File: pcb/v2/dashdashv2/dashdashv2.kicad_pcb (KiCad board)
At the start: 2 copper layers, 99 parts, among them J1 USB_B, J10 O2_CONN1, J11 BATT_CONN1, J12 OIL_CONN1, J13 OIL_TEMP1, J2 Tag connect, J3 Conn_01x04_Female, J4 Conn_01x04_Female, J5 SPEED_CONN1, J6 DISPLAY1, J7 RPM_CONN1, J8 TEMP1, J9 FUEL_CONN1, Q1 IRF540N, Q2 IRF540N, Q3 2N3904, U1 RP2040, U10 PCA9685PW, U11 MIC2940A-3.3WU, U12 SRV05-4, U13 LT4363IMS, U14 ADUM4160, U14 SRV05-4, U15 SRV05-4, U16 SRV05-4, U17 SRV05-4, U18 GL2576-3.3TA5R, U19 GL2576-5.0TA5R, U2 W25Q128JVS, U3 MCP2515-xSO, U4 TJA1042T3118, U5 TPD2E2U06, U6 SRV05-4, U7 25LCxxx, U8 SRV05-4, U9 MIC2940A-5.0WT, Y1 8MHz, Y2 12MHz

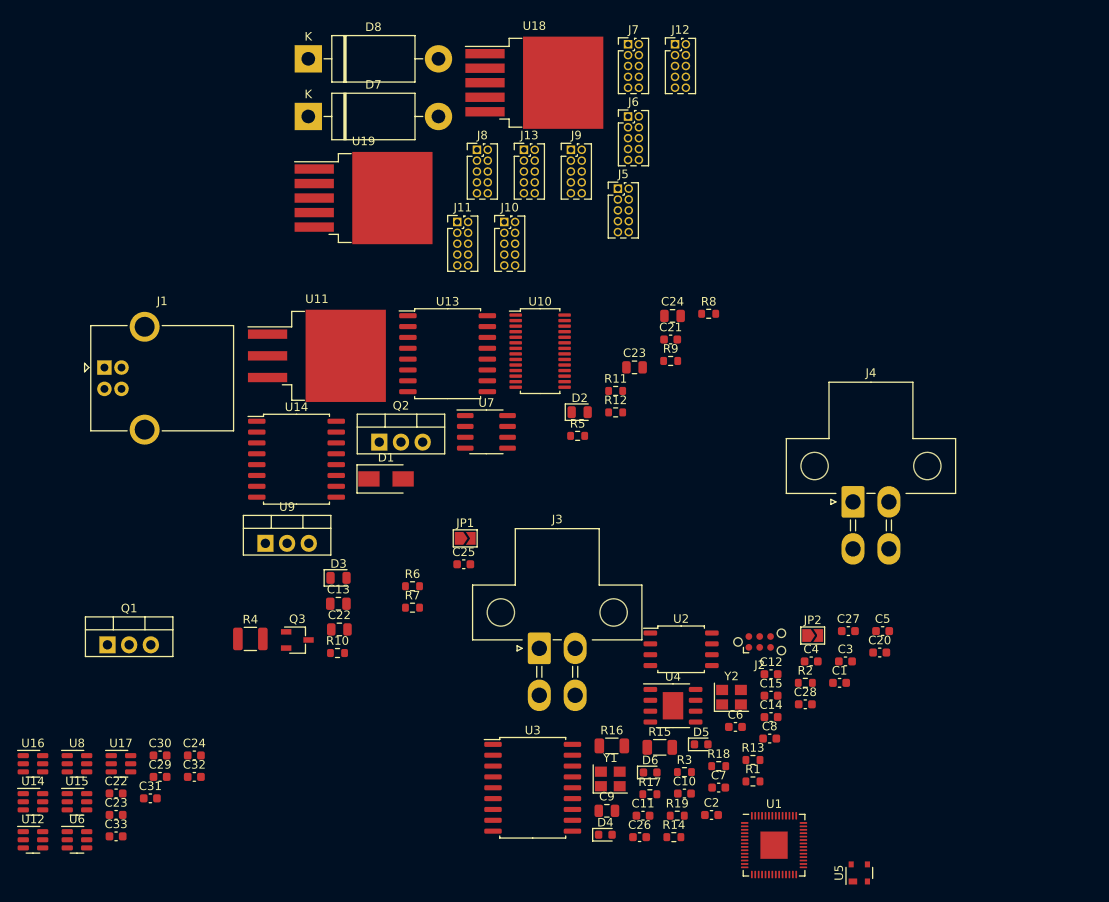
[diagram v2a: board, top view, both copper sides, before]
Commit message: routing can/usb/power/leds/flash
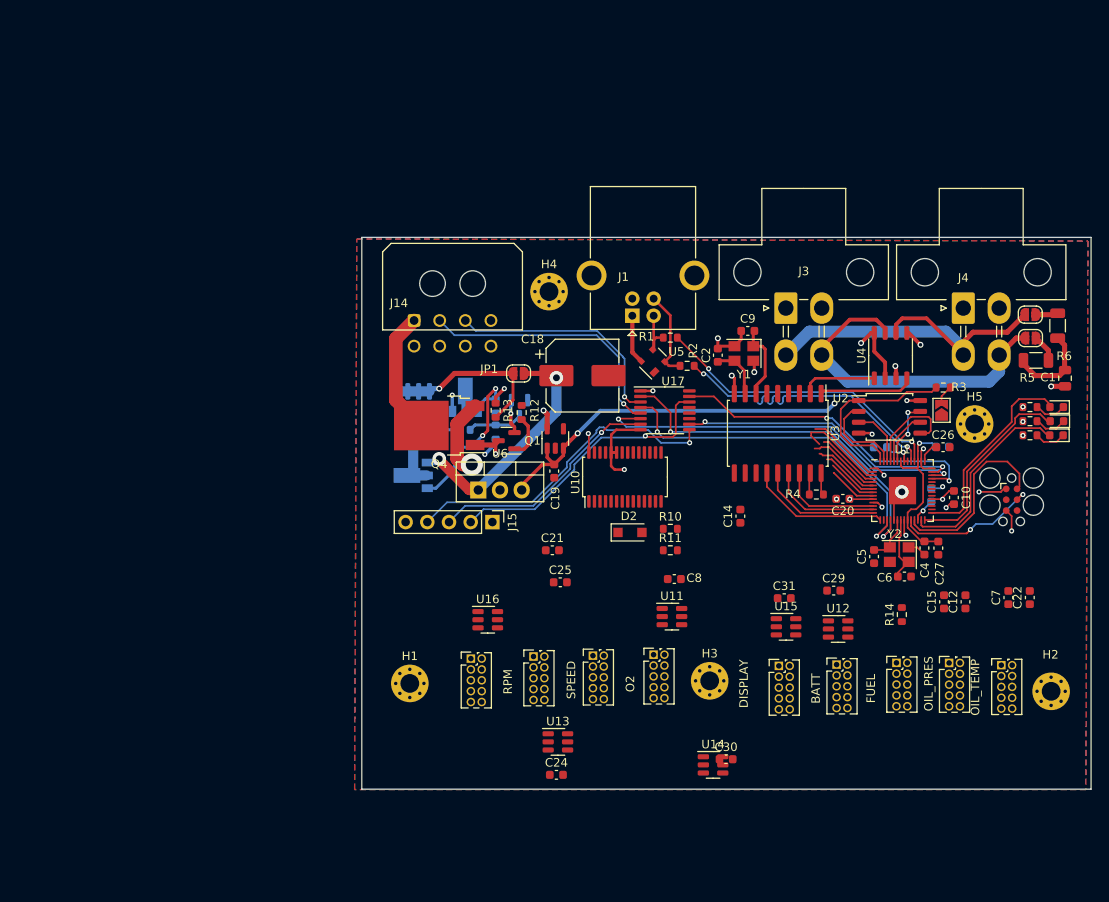
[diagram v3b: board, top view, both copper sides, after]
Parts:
- removed C13, C23: 100nF, Capacitor_SMD:C_0805_2012Metric
- removed the C22 at (136.1, 98.5)
- removed the C22 at (110.0, 117.8)
- removed C23, C33: 100nF, Capacitor_SMD:C_0603_1608Metric
- removed the C24 at (175.1, 61.8)
- removed the C24 at (119.2, 113.3)
- removed C3: 2.2uF, Capacitor_SMD:C_0603_1608Metric
- removed D3: 1N4148, Diode_SMD:D_0805_2012Metric
- removed D7, D8: 1N5822, Diode_THT:D_DO-201AD_P15.24mm_Horizontal
- removed R15, R16: 30R, Resistor_SMD:R_1206_3216Metric
- removed the U14 at (100.3, 118.7)
- removed the U14 at (131.1, 78.6)
- removed U18: GL2576-3.3TA5R, Package_TO_SOT_SMD:TO-263-5_TabPin3
- removed U19: GL2576-5.0TA5R, Package_TO_SOT_SMD:TO-263-5_TabPin3
- removed U7: 25LCxxx, Package_SO:SOIC-8_3.9x4.9mm_P1.27mm
- removed U9: MIC2940A-5.0WT, Package_TO_SOT_THT:TO-220-3_Vertical
- added C18: 120uF, Capacitor_SMD:CP_Elec_8x6.5, F.Cu at (164.6, 68.8)
- added C19: 100nF, Capacitor_SMD:C_0603_1608Metric, F.Cu at (161.3, 80.0)
- added C22: 100nF, Capacitor_SMD:C_0603_1608Metric, F.Cu at (217.0, 94.8)
- added C24: 100nF, Capacitor_SMD:C_0603_1608Metric, F.Cu at (161.5, 115.6)
- added H1: MountingHole, MountingHole:MountingHole_2.2mm_M2_Pad_Via, F.Cu at (144.4, 104.9)
- added H2: MountingHole, MountingHole:MountingHole_2.2mm_M2_Pad_Via, F.Cu at (219.5, 105.8)
- added H3: MountingHole, MountingHole:MountingHole_2.2mm_M2_Pad_Via, F.Cu at (179.5, 104.6)
- added H4: MountingHole, MountingHole:MountingHole_2.2mm_M2_Pad_Via, F.Cu at (160.7, 59.0)
- added H5: MountingHole, MountingHole:MountingHole_2.2mm_M2_Pad_Via, F.Cu at (210.5, 74.5)
- added J14: Conn_01x08, Connector_Molex:Molex_Micro-Fit_3.0_43045-0800_2x04_P3.00mm_Horizontal, F.Cu at (144.9, 62.4)
- added J15: Conn_01x05, Connector_PinHeader_2.54mm:PinHeader_1x05_P2.54mm_Vertical, F.Cu at (154.1, 86.0)
- added JP5: Jumper_2_Open, Jumper:SolderJumper-2_P1.3mm_Open_RoundedPad1.0x1.5mm, F.Cu at (217.0, 64.4)
- added JP6: Jumper_2_Open, Jumper:SolderJumper-2_P1.3mm_Open_RoundedPad1.0x1.5mm, F.Cu at (217.0, 61.7)
- added Q4: IRF9540N, Package_TO_SOT_SMD:TO-252-2, F.Cu at (147.8, 74.7)
- added Q5: MCQ9435-TP, Package_SO:SOIC-8_3.9x4.9mm_P1.27mm, B.Cu at (144.8, 73.2)
- added U14: SRV05-4, Package_TO_SOT_SMD:SOT-23-6, F.Cu at (179.9, 114.4)
- C1: value 30pF -> 4.7nF; footprint Capacitor_SMD:C_0603_1608Metric -> Capacitor_SMD:C_0805_2012Metric
- C11, C28, C32: moved to B.Cu
- C21: value 47nF -> 30pF
- C25: value 0.1uF -> 100nF
- C9: value 4.7nF -> 30pF; footprint Capacitor_SMD:C_0805_2012Metric -> Capacitor_SMD:C_0603_1608Metric
- D1: value SMAJ58CA -> BZX84C5V6LT1G; footprint Diode_SMD:D_SMA -> Package_TO_SOT_SMD:SOT-23; moved to B.Cu
- D2: value 1N4148 -> D_Zener; footprint Diode_SMD:D_0805_2012Metric -> Diode_SMD:D_SOD-123F
- J2: footprint Connector:Tag-Connect_TC2030-IDC-NL_2x03_P1.27mm_Vertical -> Connector:Tag-Connect_TC2030-IDC-FP_2x03_P1.27mm_Vertical
- JP1: footprint Jumper:SolderJumper-2_P1.3mm_Open_TrianglePad1.0x1.5mm -> Jumper:SolderJumper-2_P1.3mm_Open_RoundedPad1.0x1.5mm
- Q1: value IRF540N -> SS8050; footprint Package_TO_SOT_THT:TO-220-3_Vertical -> Package_TO_SOT_SMD:SOT-23
- Q2: value IRF540N -> 2PB1424,115; footprint Package_TO_SOT_THT:TO-220-3_Vertical -> Package_TO_SOT_SMD:SOT-89-3; moved to B.Cu
- Q3: value 2N3904 -> 2PB1424,115; footprint Package_TO_SOT_SMD:TSOT-23 -> Package_TO_SOT_SMD:SOT-89-3; moved to B.Cu
- R10: value 22r -> 5k
- R11: value 22r -> 1k
- R12: value 10K 1/10W -> 10k
- R4: value 0.01R -> 10k; footprint Resistor_SMD:R_1210_3225Metric -> Resistor_SMD:R_0603_1608Metric
- R5: value 57.6K 1/10W -> 60R; footprint Resistor_SMD:R_0603_1608Metric -> Resistor_SMD:R_1206_3216Metric
- R6: value 4.99K 1/10W -> 60R; footprint Resistor_SMD:R_0603_1608Metric -> Resistor_SMD:R_1206_3216Metric
- R7, R8: value 10R 1/10W -> 6k8; moved to B.Cu
- R9: value 1M 1/10W -> 2k7; moved to B.Cu
- U11: value MIC2940A-3.3WU -> SRV05-4; footprint Package_TO_SOT_SMD:TO-263-3_TabPin2 -> Package_TO_SOT_SMD:SOT-23-6
- U13: value LT4363IMS -> SRV05-4; footprint Package_SO:SOIC-16W_7.5x10.3mm_P1.27mm -> Package_TO_SOT_SMD:SOT-23-6
- U17: value SRV05-4 -> 4050; footprint Package_TO_SOT_SMD:SOT-23-6 -> Package_SO:TSSOP-16_4.4x5mm_P0.65mm
- U6: value SRV05-4 -> LM7805_TO220; footprint Package_TO_SOT_SMD:SOT-23-6 -> Package_TO_SOT_THT:TO-220-3_Vertical
- U8: value SRV05-4 -> LP5907MFX-3.3; footprint Package_TO_SOT_SMD:SOT-23-6 -> Package_TO_SOT_SMD:SOT-23-5
- moved U12 97.4 mm to (194.5, 98.5)
- moved C32 89.1 mm to (199.5, 77.2)
- moved U15 85.5 mm to (188.4, 98.2)
- moved C29 81.8 mm to (194.0, 94.0)
- moved R6 81.4 mm to (220.2, 63.0), turned to 90 degrees
- moved J12 79.2 mm to (207.5, 102.5)
- moved C31 77.8 mm to (188.2, 94.9)
- moved J6 77.7 mm to (213.6, 102.7)
- moved U17 75.9 mm to (174.2, 72.9)
- moved J7 74.2 mm to (151.5, 102.0)
- moved J8 73.5 mm to (194.3, 102.7)
- moved D4 70.5 mm to (220.1, 75.8), turned to 180 degrees
- moved R4 68.4 mm to (192.0, 82.8)
- moved U8 67.7 mm to (161.4, 76.2), turned to 90 degrees
- moved C30 66.3 mm to (181.4, 113.7)
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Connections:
- net /PWM_BACK_FUEl renamed PWM_BACK_FUEl
- net Net-(R14-Pad1) renamed /QSPI_SS
- net Net-(U1-Pad51) renamed /QSPI_SD3
- net Net-(U1-Pad52) renamed /QSPI_SCLK
- net Net-(U1-Pad53) renamed /QSPI_SD0
- net Net-(U1-Pad54) renamed /QSPI_SD2
- net Net-(U1-Pad55) renamed /QSPI_SD1
- C1 pad 1: GND -> Net-(C1-Pad1)
- C1 pad 2: /CAN_CLOCK_A -> GND
- C2 pad 2: /CAN_CLOCK_B -> /CAN/CAN_CLOCK_A
- C21 pad 1: Net-(C21-Pad1) -> GND
- C21 pad 2: GND -> +3V3
- C25 pad 1: Net-(C25-Pad1) -> GND
- C25 pad 2: GND -> +3V3
- C28 pad 1: unconnected-(C28-Pad1) -> +1V1
- C7 pad 2: +3V3 -> Net-(C7-Pad2)
- C8 pad 1: GND -> Net-(C7-Pad2)
- C8 pad 2: +3V3 -> GND
- C9 pad 1: Net-(C9-Pad1) -> GND
- C9 pad 2: GND -> /CAN/CAN_CLOCK_B
- D1 pad 1: Net-(D1-Pad1) -> GND
- D1 pad 2: GND -> unconnected-(D1-Pad2)
- D2 pad 2: +12VA -> GND
- J10 pad 1: +5V -> +12LF
- J10 pad 2: +5V -> +12LF
- J10 pad 3: /CLK -> CLK
- J10 pad 4: /O2_CS -> O2_CS
- J10 pad 5: /MISO -> MISO
- J10 pad 7: /MOSI -> MOSI
- J10 pad 8: /PWM_BACK_O2 -> PWM_BACK_O2
- J11 pad 1: +5V -> +12LF
- J11 pad 2: +5V -> +12LF
- J11 pad 3: /CLK -> CLK
- J11 pad 4: /BATT_CS -> BATT_CS
- J11 pad 5: /MISO -> MISO
- J11 pad 7: /MOSI -> MOSI
- J11 pad 8: /PWM_BACK_BATT -> PWM_BACK_BATT
- J12 pad 1: +5V -> +12LF
- J12 pad 2: +5V -> +12LF
- J12 pad 3: /CLK -> CLK
- J12 pad 4: /OIL_CS -> OIL_CS
- J12 pad 5: /MISO -> MISO
- J12 pad 7: /MOSI -> MOSI
- J12 pad 8: /PWM_BACK_OIL -> PWM_BACK_OIL
- J13 pad 1: +5V -> +12LF
- J13 pad 2: +5V -> +12LF
- J13 pad 3: /CLK -> CLK
- J13 pad 4: /OIL_TEMP_CS -> OIL_TEMP_CS
- J13 pad 5: /MISO -> MISO
- J13 pad 7: /MOSI -> MOSI
- J13 pad 8: /PWM_BACK_OIL_TEMP -> PWM_BACK_OIL_TEMP
- J5 pad 1: +5V -> +12LF
- J5 pad 2: +5V -> +12LF
- J5 pad 3: /CLK -> CLK
- J5 pad 4: /SPEED_CS -> SPEED_CS
- J5 pad 5: /MISO -> MISO
- J5 pad 6: /PWM_SPEED1 -> PWM_SPEED1
- J5 pad 7: /MOSI -> MOSI
- J5 pad 8: /PWM_SPEED2 -> PWM_SPEED2
- J6 pad 1: +5V -> +12LF
- J6 pad 2: +5V -> +12LF
- J6 pad 3: /CLK -> CLK
- J6 pad 4: /DISPLAY_CS -> DISPLAY_CS
- J6 pad 5: /MISO -> MISO
- J6 pad 7: /MOSI -> MOSI
- J6 pad 8: /PWM_BACK_DISPLAY -> PWM_BACK_DISPLAY
- J7 pad 1: +5V -> +12LF
- J7 pad 2: +5V -> +12LF
- J7 pad 3: /CLK -> CLK
- J7 pad 4: /RPM_CS -> RPM_CS
- J7 pad 5: /MISO -> MISO
- J7 pad 7: /MOSI -> MOSI
- J7 pad 8: /PWM_BACK_RPM -> PWM_BACK_RPM
- J8 pad 1: +5V -> +12LF
- J8 pad 2: +5V -> +12LF
- J8 pad 3: /CLK -> CLK
- J8 pad 4: /TEMP_CS -> TEMP_CS
- J8 pad 5: /MISO -> MISO
- J8 pad 7: /MOSI -> MOSI
- J8 pad 8: /PWM_BACK_TEMP -> PWM_BACK_TEMP
- J9 pad 1: +5V -> +12LF
- J9 pad 2: +5V -> +12LF
- J9 pad 3: /CLK -> CLK
- J9 pad 4: /FUEL_CS -> FUEL_CS
- J9 pad 5: /MISO -> MISO
- J9 pad 7: /MOSI -> MOSI
- JP1 pad 1: +12VA -> 12V_BATT
- Q1 pad 2: Net-(D1-Pad1) -> GND
- Q1 pad 3: +12VA -> Net-(Q1-Pad3)
- Q2 pad 1: Net-(Q2-Pad1) -> +12V
- Q2 pad 3: Net-(D1-Pad1) -> Net-(Q3-Pad1)
- Q3 pad 1: +12VA -> Net-(Q3-Pad1)
- Q3 pad 2: Net-(D2-Pad1) -> Net-(Q2-Pad2)
- R1 pad 1: Net-(R1-Pad1) -> /D+
- R10 pad 1: /D+ -> +12V
- R10 pad 2: /d+ -> Net-(D2-Pad1)
- R11 pad 1: /D- -> Net-(D2-Pad1)
- R11 pad 2: /d- -> GND
- R12 pad 1: Net-(D2-Pad1) -> Net-(Q1-Pad1)
- R12 pad 2: Net-(D3-Pad1) -> 12V_ENABLE
- R13 pad 1: Net-(R13-Pad1) -> Net-(Q1-Pad3)
- R13 pad 2: +3V3 -> 12V_BATT
- R2 pad 2: Net-(R2-Pad2) -> /D-
- R4 pad 1: +12V -> Net-(R4-Pad1)
- R4 pad 2: Net-(Q2-Pad2) -> +3V3
- R5 pad 1: +12V -> Net-(C1-Pad1)
- R5 pad 2: Net-(R5-Pad2) -> Net-(JP5-Pad2)
- R6 pad 1: GND -> Net-(C1-Pad1)
- R6 pad 2: Net-(R5-Pad2) -> Net-(JP6-Pad2)
- R7 pad 1: Net-(Q1-Pad1) -> Net-(Q3-Pad1)
- R7 pad 2: Net-(Q3-Pad3) -> GND
- R8 pad 1: Net-(Q2-Pad1) -> Net-(Q3-Pad3)
- R8 pad 2: Net-(C21-Pad1) -> Net-(D1-Pad3)
- R9 pad 1: Net-(C21-Pad1) -> Net-(Q2-Pad2)
- R9 pad 2: Net-(Q3-Pad3) -> Net-(D1-Pad3)
- U1 pad 11: unconnected-(U1-Pad11) -> OIL_TEMP_CS
- U1 pad 12: /CLK2 -> CS_CAN
- U1 pad 13: /MISO2 -> MOSI2
- U1 pad 14: /MOSI2 -> MISO2
- U1 pad 15: /CS_CAN -> CLK2
- U1 pad 17: unconnected-(U1-Pad17) -> 12V_ACC
- U1 pad 18: unconnected-(U1-Pad18) -> 12V_LIGHT
- U1 pad 2: unconnected-(U1-Pad2) -> RPM_CS
- U1 pad 3: unconnected-(U1-Pad3) -> FUEL_CS
- U1 pad 30: /CLK -> CLK
- U1 pad 31: /MISO -> MISO
- U1 pad 32: /MOSI -> MOSI
- U1 pad 35: /I2C1_SCL -> I2C1_SCL
- U1 pad 36: /I2C1_SDA -> I2C1_SDA
- U1 pad 37: unconnected-(U1-Pad37) -> 12V_ENABLE
- U1 pad 38: unconnected-(U1-Pad38) -> Net-(D2-Pad1)
- U1 pad 39: unconnected-(U1-Pad39) -> ENCODER_A
- U1 pad 4: unconnected-(U1-Pad4) -> SPEED_CS
- U1 pad 40: unconnected-(U1-Pad40) -> ENCODER_B
- U1 pad 41: unconnected-(U1-Pad41) -> ENCODER_C
- U1 pad 46: Net-(R1-Pad1) -> /D+
- U1 pad 47: Net-(R2-Pad2) -> /D-
- U1 pad 5: unconnected-(U1-Pad5) -> O2_CS
- U1 pad 6: unconnected-(U1-Pad6) -> OIL_CS
- U1 pad 7: unconnected-(U1-Pad7) -> BATT_CS
- U1 pad 8: unconnected-(U1-Pad8) -> DISPLAY_CS
- U1 pad 9: unconnected-(U1-Pad9) -> TEMP_CS
- U10 pad 10: /PWM_FUEL2 -> PWM_BACK_DISPLAY
- U10 pad 11: /PWM_BAR1 -> PWM_BACK_OIL
- U10 pad 12: /PWM_BAR2 -> PWM_BACK_O2
- U10 pad 13: /PWM_BAR3 -> PWM_BACK_TEMP
- U10 pad 15: /PWM_VEL -> PWM_BACK_BATT
- U10 pad 16: /PWM_OD -> PWM_BACK_OIL_TEMP
- U10 pad 17: /PWM_BACK_1 -> unconnected-(U10-Pad17)
- U10 pad 18: /PWM_BACK_2 -> unconnected-(U10-Pad18)
- U10 pad 26: /I2C1_SDA -> I2C1_SCL
- U10 pad 27: /I2C1_SCL -> I2C1_SDA
- U10 pad 6: /PWM_BACK_RPM -> PWM_BACK_RPM
- U10 pad 7: /PWM_SPEED1 -> PWM_BACK_FUEL
- U10 pad 8: /PWM_SPEED2 -> PWM_SPEED1
- U10 pad 9: /PWM_FUEL1 -> PWM_SPEED2
- U11 pad 1: +12V -> CLK
- U11 pad 3: +3V3 -> MISO
- U12 pad 1: /PWM_BACK_RPM -> BATT_CS
- U12 pad 3: /PWM_BACK_FUEL -> OIL_TEMP_CS
- U12 pad 4: /PWM_SPEED1 -> OIL_CS
- U12 pad 6: /PWM_SPEED2 -> TEMP_CS
- U13 pad 1: Net-(R5-Pad2) -> PWM_BACK_RPM
- U13 pad 2: +12V -> GND
- U13 pad 3: Net-(Q2-Pad2) -> PWM_BACK_FUEL
- U13 pad 4: Net-(C21-Pad1) -> PWM_SPEED1
- U13 pad 5: Net-(D1-Pad1) -> +3V3
- U13 pad 6: unconnected-(U13-Pad6) -> PWM_SPEED2
- U15 pad 1: /PWM_BACK_DISPLAY -> PWM_BACK_DISPLAY
- U15 pad 3: /PWM_BACK_OIL -> PWM_BACK_OIL
- U15 pad 4: /PWM_BACK_O2 -> PWM_BACK_O2
- U15 pad 6: /PWM_BACK_TEMP -> PWM_BACK_TEMP
- U16 pad 1: /RPM_CS -> RPM_CS
- U16 pad 3: /SPEED_CS -> SPEED_CS
- U16 pad 4: /FUEL_CS -> FUEL_CS
- U16 pad 6: /O2_CS -> O2_CS
- U17 pad 1: /PWM_BACK_BATT -> +3V3
- U17 pad 2: GND -> 12V_LIGHT
- U17 pad 3: /PWM_BACK_OIL_TEMP -> Net-(J14-Pad3)
- U17 pad 4: unconnected-(U17-Pad4) -> 12V_ACC
- U17 pad 5: +3V3 -> Net-(J14-Pad2)
- U17 pad 6: unconnected-(U17-Pad6) -> ENCODER_B
- U3 pad 13: /CLK2 -> CLK2
- U3 pad 14: /MISO2 -> MISO2
- U3 pad 15: /MOSI2 -> MOSI2
- U3 pad 16: /CS_CAN -> CS_CAN
- U3 pad 17: Net-(R13-Pad1) -> Net-(R4-Pad1)
- U3 pad 7: /CAN_CLOCK_B -> /CAN/CAN_CLOCK_B
- U3 pad 8: /CAN_CLOCK_A -> /CAN/CAN_CLOCK_A
- U6 pad 1: /CLK -> +12V
- U6 pad 3: /MISO -> +5V
- U8 pad 1: /BATT_CS -> +5V
- U8 pad 3: /OIL_TEMP_CS -> +5V
- U8 pad 4: /OIL_CS -> unconnected-(U8-Pad4)
- Y1 pad 1: /CAN_CLOCK_B -> /CAN/CAN_CLOCK_B
- Y1 pad 3: /CAN_CLOCK_A -> /CAN/CAN_CLOCK_A
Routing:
- net GND: track 0.00 -> 56.7 mm, vias 0 -> 16
- net +5V: track 0.00 -> 54.3 mm, vias 0 -> 3
- net CAN-: track 0.00 -> 45.8 mm
- net ENCODER_B: track 0.00 -> 44.9 mm, vias 0 -> 2
- net 12V_BATT: track 0.00 -> 44.0 mm, vias 0 -> 1
- net 12V_LIGHT: track 0.00 -> 42.6 mm, vias 0 -> 2
- net 12V_ACC: track 0.00 -> 42.3 mm, vias 0 -> 2
- net CAN+: track 0.00 -> 39.0 mm
- net Net-(J15-Pad4): track 0.00 -> 38.1 mm, vias 0 -> 1
- net ENCODER_A: track 0.00 -> 37.7 mm, vias 0 -> 2
- net +3V3: track 0.00 -> 35.6 mm, vias 0 -> 13
- net /D+: track 0.00 -> 35.1 mm, vias 0 -> 2
- net /D-: track 0.00 -> 34.6 mm, vias 0 -> 2
- net Net-(J15-Pad2): track 0.00 -> 33.8 mm, vias 0 -> 1
- net ENCODER_C: track 0.00 -> 33.5 mm, vias 0 -> 2
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- added copper zone on In2.Cu, net +12LF
- added copper zone on In1.Cu, net +3V3
- added copper zone on B.Cu, net GND
- added copper zone on F.Cu, net GND
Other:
- board outline added: 85.4 x 64.6 mm
- copper layers 2 -> 4
- board text added: "BATT"
- board text added: "DISPLAY"
- board text added: "FUEL"
- board text added: "O2"
- board text added: "OIL_PRES"
- board text added: "OIL_TEMP"
- board text added: "RPM"
- board text added: "SPEED"

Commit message: routing
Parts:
- removed C14: 100nF, Capacitor_SMD:C_0603_1608Metric
- C12, C15, C7, C8: moved to B.Cu
- C32: moved to F.Cu
- moved J13 57.4 mm to (216.0, 95.9)
- moved C32 49.1 mm to (152.0, 89.9), turned to 90 degrees
- moved J5 39.3 mm to (162.6, 95.9)
- moved C8 33.3 mm to (201.0, 71.5), turned to 180 degrees
- moved C30 31.3 mm to (182.0, 82.4)
- moved R14 30.1 mm to (206.0, 67.0)
- moved U14 29.5 mm to (182.1, 85.0)
- moved C24 28.7 mm to (167.7, 87.6)
- moved C7 24.9 mm to (204.5, 72.0)
- moved J12 23.9 mm to (184.5, 95.9)
- moved U13 22.0 mm to (167.6, 90.6)
- moved C25 18.9 mm to (180.3, 88.3)
- moved C22 16.9 mm to (216.5, 77.9), turned to 0 degrees
- moved C15 15.9 mm to (209.1, 79.6), turned to -90 degrees
- moved J8 15.2 mm to (208.0, 95.9)
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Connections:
- C7 pad 2: Net-(C7-Pad2) -> +3V3
- C8 pad 1: Net-(C7-Pad2) -> +3V3
- U1 pad 27: /LED_GREEN -> CLK
- U1 pad 28: /LED_BLUE -> MISO
- U1 pad 29: /LED_RED -> MOSI
- U1 pad 30: CLK -> /LED_GREEN
- U1 pad 31: MISO -> /LED_BLUE
- U1 pad 32: MOSI -> /LED_RED
- U10 pad 7: PWM_BACK_FUEL -> PWM_BACK_FUEl
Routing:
- net MOSI: track 0.00 -> 147.7 mm, vias 0 -> 2
- net MISO: track 0.00 -> 143.7 mm, vias 0 -> 2
- net CLK: track 0.00 -> 135.1 mm, vias 0 -> 4
- net Net-(D2-Pad1): track 0.00 -> 68.0 mm, vias 0 -> 3
- net TEMP_CS: track 5.73 -> 68.5 mm, vias 0 -> 1
- net RPM_CS: track 8.88 -> 70.7 mm, vias 0 -> 2
- net 12V_ENABLE: track 0.00 -> 61.7 mm, vias 0 -> 2
- net PWM_BACK_OIL_TEMP: track 0.00 -> 61.1 mm, vias 0 -> 2
- net O2_CS: track 8.60 -> 69.7 mm, vias 0 -> 3
- net SPEED_CS: track 7.56 -> 68.5 mm, vias 0 -> 2
- net PWM_BACK_TEMP: track 0.00 -> 59.7 mm, vias 0 -> 2
- net DISPLAY_CS: track 6.02 -> 64.2 mm, vias 0 -> 3
- net BATT_CS: track 6.86 -> 63.4 mm, vias 0 -> 2
- net OIL_CS: track 7.83 -> 62.5 mm, vias 0 -> 2
- net FUEL_CS: track 11.1 -> 64.2 mm, vias 0 -> 1
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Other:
- board size 85.4 x 64.6 mm -> 85.4 x 50.1 mm
- board text added: "Churrosoft"
- board text added: "DashDash Mainboard v1"
- board text added: "TEMP"
